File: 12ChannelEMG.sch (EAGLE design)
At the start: 24 parts

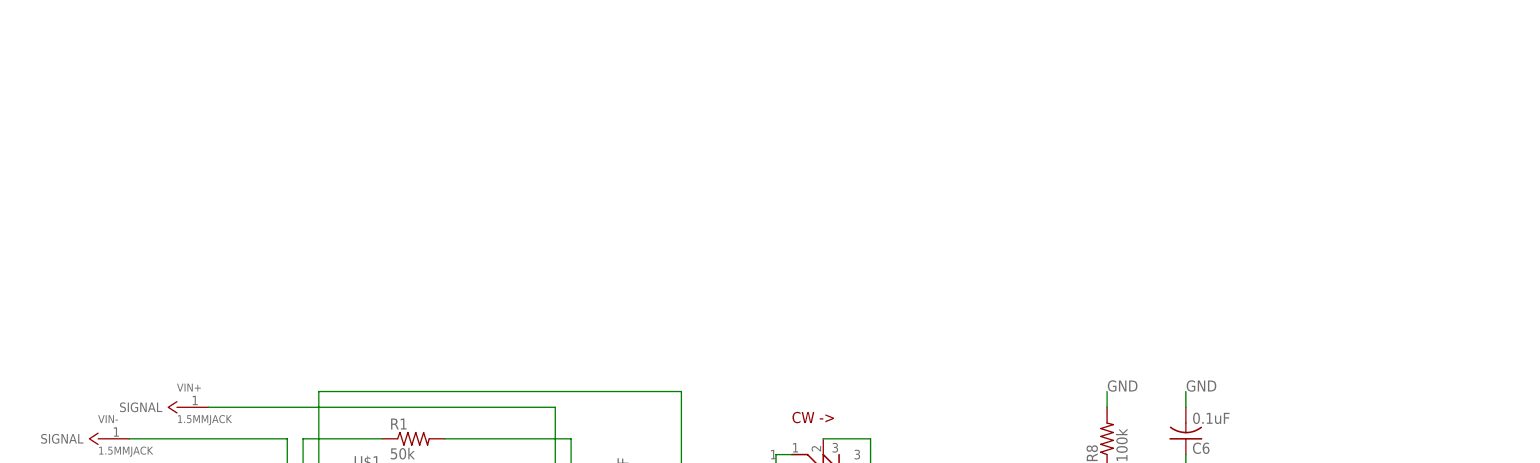
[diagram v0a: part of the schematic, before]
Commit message: Duplicated first channel to make second channel
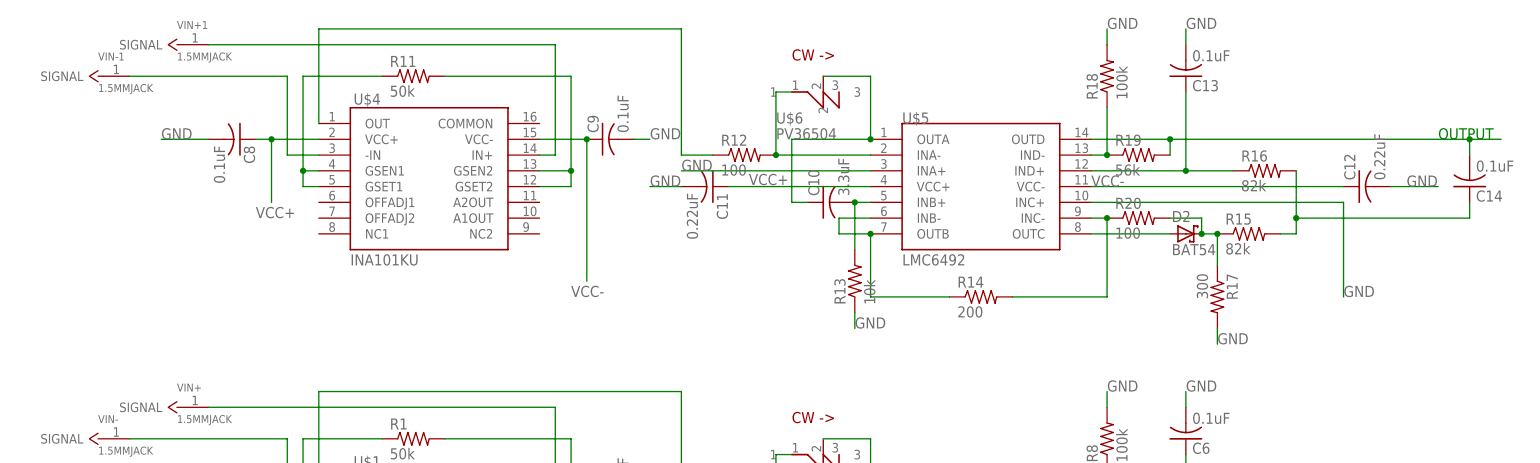
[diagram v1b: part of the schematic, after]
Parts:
- added C10: 3.3uF, resistor:C-USC1206K
- added C11, C12: 0.22uF, rcl:C-USC0603K
- added C13, C14, C8, C9: 0.1uF, resistor:C-USC1206K
- added D2: BAT54, diode:BAT54
- added R11: 50k, rcl:R-US_R0805
- added R12, R20: 100, resistor:R-US_R0603
- added R13: 10k, rcl:R-US_R0603
- added R14: 200, rcl:R-US_R0603
- added R15, R16: 82k, resistor:R-US_R0603
- added R17: 300, resistor:R-US_R0603
- added R18: 100k, resistor:R-US_R0603
- added R19: 56k, resistor:R-US_R0603
- added U$4: INA101KU, 12-ChannelEMG:INA101KUINA101KU
- added U$5: LMC6492, 12-ChannelEMG:LMC6492
- added U$6: PV36504, 12-ChannelEMG:PV36
- added VIN+1, VIN-1: 1.5MMJACK, 12-ChannelEMG:1.5MMJACK
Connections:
- new net N$13: R11.2, U$4.GSEN2, U$4.GSET2
- new net N$20: U$4.-IN, VIN-1.SIGNAL
- new net N$21: R12.2, U$5.INA-, U$6.1
- new net N$22: R12.1, U$4.OUT
- new net N$23: C10.1, U$5.OUTA, U$6.2
- new net N$24: C10.2, R13.2, U$5.INB+
- new net N$25: R14.1, U$5.INB-, U$5.OUTB
- new net N$26: R14.2, R20.1, U$5.INC-
- new net N$27: D2.A, U$5.OUTC
- new net N$28: C13.1, R16.1, U$5.IND+
- new net N$29: D2.C, R15.1, R17.1, R20.2
- new net N$30: C14.2, R19.2, U$5.OUTD
- new net N$31: R18.1, R19.1, U$5.IND-
- new net N$32: C14.1, R15.2, R16.2
- new net N$33: R11.1, U$4.GSEN1, U$4.GSET1
- new net N$34: U$4.IN+, VIN+1.SIGNAL
- net GND: now also C11.2, C12.2, C13.2, C8.2, C9.2, R13.1, R17.2, R18.2, U$5.INA+, U$5.INC+
- net VCC+: now also C11.1, C8.1, U$4.VCC+, U$5.VCC+
- net VCC-: now also C12.1, C9.1, U$4.VCC-, U$5.VCC-

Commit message: Three Channels
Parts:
- added C15, C16, C20, C21: 0.1uF, resistor:C-USC1206K
- added C17: 3.3uF, resistor:C-USC1206K
- added C18, C19: 0.22uF, rcl:C-USC0603K
- added D3: BAT54, diode:BAT54
- added R21: 50k, rcl:R-US_R0805
- added R22, R30: 100, resistor:R-US_R0603
- added R23: 10k, rcl:R-US_R0603
- added R24: 200, rcl:R-US_R0603
- added R25, R26: 82k, resistor:R-US_R0603
- added R27: 300, resistor:R-US_R0603
- added R28: 100k, resistor:R-US_R0603
- added R29: 56k, resistor:R-US_R0603
- added U$7: INA101KU, 12-ChannelEMG:INA101KUINA101KU
- added U$8: LMC6492, 12-ChannelEMG:LMC6492
- added U$9: PV36504, 12-ChannelEMG:PV36
- added VIN+2, VIN-2: 1.5MMJACK, 12-ChannelEMG:1.5MMJACK
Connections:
- new net N$35: R21.2, U$7.GSEN2, U$7.GSET2
- new net N$36: U$7.-IN, VIN-2.SIGNAL
- new net N$37: R22.2, U$8.INA-, U$9.1
- new net N$38: R22.1, U$7.OUT
- new net N$39: C17.1, U$8.OUTA, U$9.2
- new net N$40: C17.2, R23.2, U$8.INB+
- new net N$41: R24.1, U$8.INB-, U$8.OUTB
- new net N$42: R24.2, R30.1, U$8.INC-
- new net N$43: D3.A, U$8.OUTC
- new net N$44: C20.1, R26.1, U$8.IND+
- new net N$45: D3.C, R25.1, R27.1, R30.2
- new net N$46: C21.2, R29.2, U$8.OUTD
- new net N$47: R28.1, R29.1, U$8.IND-
- new net N$48: C21.1, R25.2, R26.2
- new net N$49: R21.1, U$7.GSEN1, U$7.GSET1
- new net N$50: U$7.IN+, VIN+2.SIGNAL
- net GND: now also C15.2, C16.2, C18.2, C19.2, C20.2, R23.1, R27.2, R28.2, U$8.INA+, U$8.INC+
- net VCC+: now also C15.1, C18.1, U$7.VCC+, U$8.VCC+
- net VCC-: now also C16.1, C19.1, U$7.VCC-, U$8.VCC-

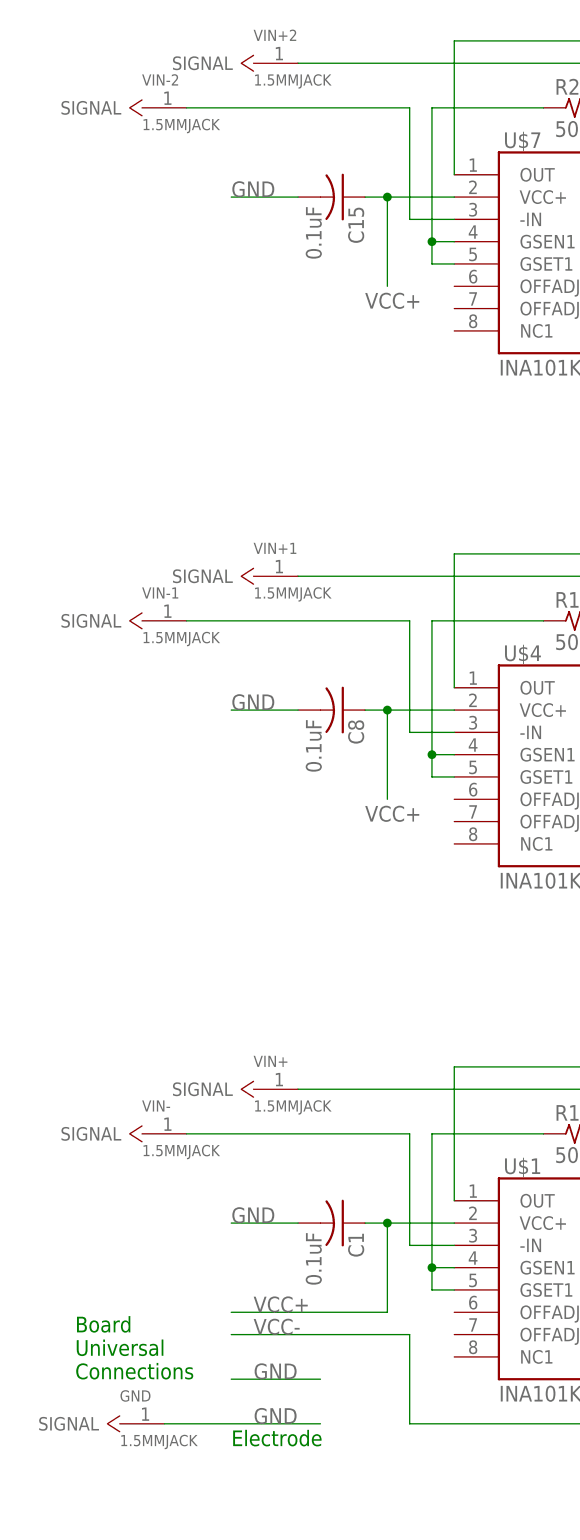
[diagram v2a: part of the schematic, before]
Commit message: Removed old connectors
Added ground jumper for ground electrode
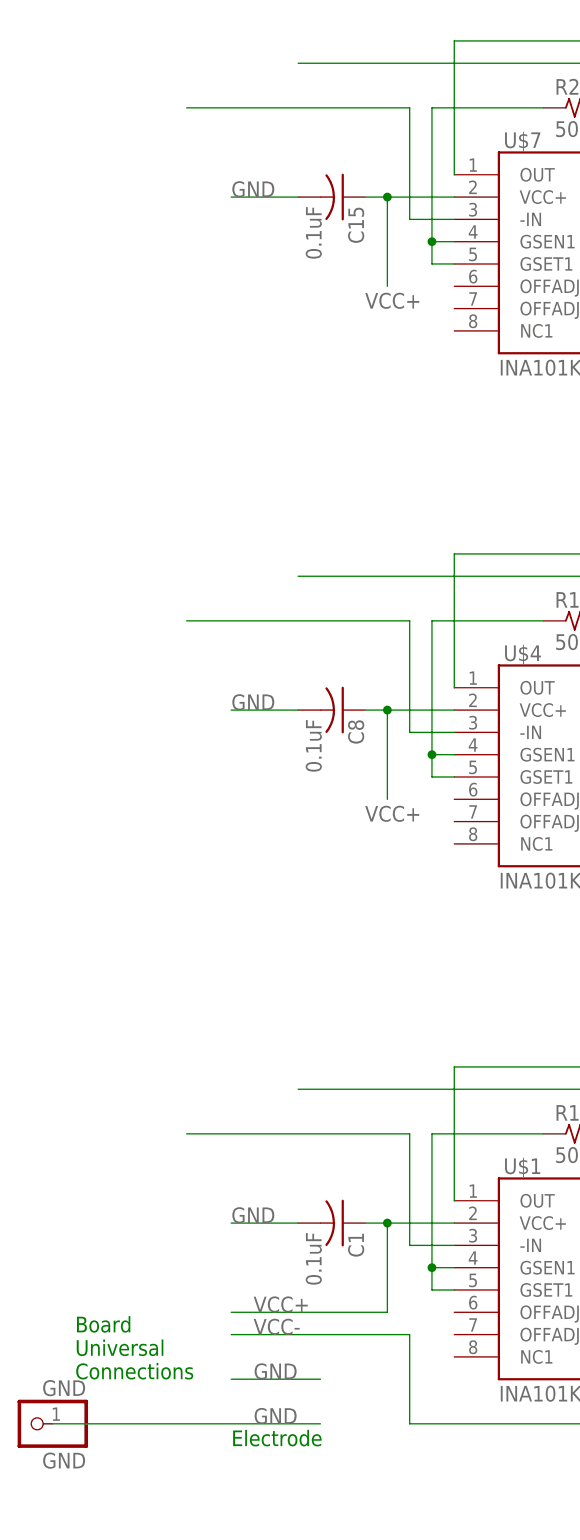
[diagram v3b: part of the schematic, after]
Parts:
- removed VIN+, VIN+1, VIN+2, VIN-, VIN-1, VIN-2: 1.5MMJACK, 12-ChannelEMG:1.5MMJACK
- GND: value 1.5MMJACK -> GND; device 12-ChannelEMG:1.5MMJACK -> pinhead:PINHD-1X1
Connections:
- net GND: now also GND.1; no longer GND.SIGNAL
- net N$20: no longer VIN-1.SIGNAL
- net N$34: no longer VIN+1.SIGNAL
- net N$36: no longer VIN-2.SIGNAL
- net N$50: no longer VIN+2.SIGNAL
- net N$6: no longer VIN-.SIGNAL
- net N$7: no longer VIN+.SIGNAL
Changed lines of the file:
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@@
 <part name="R9" library="resistor" deviceset="R-US_" device="R0603" value="56k"/>
 <part name="R10" library="resistor" deviceset="R-US_" device="R0603" value="100"/>
-<part name="VIN+" library="12-ChannelEMG" deviceset="1.5MMJACK" device=""/>
-<part name="VIN-" library="12-ChannelEMG" deviceset="1.5MMJACK" device=""/>
-<part name="GND" library="12-ChannelEMG" deviceset="1.5MMJACK" device=""/>
 <part name="U$4" library="12-ChannelEMG" deviceset="INA101KU" device="INA101KU" value="INA101KU"/>
 <part name="R11" library="rcl" deviceset="R-US_" device="R0805" value="50k"/>
@@
 <part name="R19" library="resistor" deviceset="R-US_" device="R0603" value="56k"/>
 <part name="R20" library="resistor" deviceset="R-US_" device="R0603" value="100"/>
-<part name="VIN+1" library="12-ChannelEMG" deviceset="1.5MMJACK" device=""/>
-<part name="VIN-1" library="12-ChannelEMG" deviceset="1.5MMJACK" device=""/>
 <part name="U$7" library="12-ChannelEMG" deviceset="INA101KU" device="INA101KU" value="INA101KU"/>
 <part name="R21" library="rcl" deviceset="R-US_" device="R0805" value="50k"/>
@@
 <part name="R29" library="resistor" deviceset="R-US_" device="R0603" value="56k"/>
 <part name="R30" library="resistor" deviceset="R-US_" device="R0603" value="100"/>
-<part name="VIN+2" library="12-ChannelEMG" deviceset="1.5MMJACK" device=""/>
-<part name="VIN-2" library="12-ChannelEMG" deviceset="1.5MMJACK" device=""/>
+<part name="GND" library="pinhead" deviceset="PINHD-1X1" device="" value="GND"/>
 </parts>
 <sheets>
@@
 <instance part="R9" gate="G$1" x="139.7" y="45.72"/>
 <instance part="R10" gate="G$1" x="139.7" y="35.56"/>
-<instance part="VIN+" gate="G$1" x="-17.78" y="63.5"/>
-<instance part="VIN-" gate="G$1" x="-30.48" y="58.42"/>
-<instance part="GND" gate="G$1" x="-33.02" y="25.4"/>
 <instance part="U$4" gate="G$1" x="25.4" y="101.6"/>
 <instance part="R11" gate="G$1" x="22.86" y="116.84"/>
@@
 <instance part="R19" gate="G$1" x="139.7" y="104.14"/>
 <instance part="R20" gate="G$1" x="139.7" y="93.98"/>
-<instance part="VIN+1" gate="G$1" x="-17.78" y="121.92"/>
-<instance part="VIN-1" gate="G$1" x="-30.48" y="116.84"/>
 <instance part="U$7" gate="G$1" x="25.4" y="160.02"/>
 <instance part="R21" gate="G$1" x="22.86" y="175.26"/>
@@
 <instance part="R29" gate="G$1" x="139.7" y="162.56"/>
 <instance part="R30" gate="G$1" x="139.7" y="152.4"/>
-<instance part="VIN+2" gate="G$1" x="-17.78" y="180.34"/>
-<instance part="VIN-2" gate="G$1" x="-30.48" y="175.26"/>
+<instance part="GND" gate="G$1" x="-40.64" y="25.4" rot="MR0"/>
 </instances>
 <busses>
@@
 <wire x1="-17.78" y1="30.48" x2="-7.62" y2="30.48" width="0.1524" layer="91"/>
 <label x="-15.24" y="30.48" size="1.778" layer="95"/>
-<wire x1="-25.4" y1="25.4" x2="-7.62" y2="25.4" width="0.1524" layer="91"/>
+<wire x1="-38.1" y1="25.4" x2="-7.62" y2="25.4" width="0.1524" layer="91"/>
 <label x="-15.24" y="25.4" size="1.778" layer="95"/>
-<pinref part="GND" gate="G$1" pin="SIGNAL"/>
+<pinref part="GND" gate="G$1" pin="1"/>
 </segment>
 <segment>
@@
 <wire x1="2.54" y1="45.72" x2="2.54" y2="58.42" width="0.1524" layer="91"/>
 <wire x1="2.54" y1="58.42" x2="-22.86" y2="58.42" width="0.1524" layer="91"/>
-<pinref part="VIN-" gate="G$1" pin="SIGNAL"/>
 </segment>
 </net>
@@
 <wire x1="43.18" y1="45.72" x2="45.72" y2="45.72" width="0.1524" layer="91"/>
 <wire x1="45.72" y1="45.72" x2="45.72" y2="63.5" width="0.1524" layer="91"/>
-<pinref part="VIN+" gate="G$1" pin="SIGNAL"/>
 <wire x1="45.72" y1="63.5" x2="-10.16" y2="63.5" width="0.1524" layer="91"/>
 </segment>
@@
 <wire x1="2.54" y1="104.14" x2="2.54" y2="116.84" width="0.1524" layer="91"/>
 <wire x1="2.54" y1="116.84" x2="-22.86" y2="116.84" width="0.1524" layer="91"/>
-<pinref part="VIN-1" gate="G$1" pin="SIGNAL"/>
 </segment>
 </net>
@@
 <wire x1="43.18" y1="104.14" x2="45.72" y2="104.14" width="0.1524" layer="91"/>
 <wire x1="45.72" y1="104.14" x2="45.72" y2="121.92" width="0.1524" layer="91"/>
-<pinref part="VIN+1" gate="G$1" pin="SIGNAL"/>
 <wire x1="45.72" y1="121.92" x2="-10.16" y2="121.92" width="0.1524" layer="91"/>
 </segment>
@@
 <wire x1="2.54" y1="162.56" x2="2.54" y2="175.26" width="0.1524" layer="91"/>
 <wire x1="2.54" y1="175.26" x2="-22.86" y2="175.26" width="0.1524" layer="91"/>
-<pinref part="VIN-2" gate="G$1" pin="SIGNAL"/>
 </segment>
 </net>
@@
 <wire x1="43.18" y1="162.56" x2="45.72" y2="162.56" width="0.1524" layer="91"/>
 <wire x1="45.72" y1="162.56" x2="45.72" y2="180.34" width="0.1524" layer="91"/>
-<pinref part="VIN+2" gate="G$1" pin="SIGNAL"/>
 <wire x1="45.72" y1="180.34" x2="-10.16" y2="180.34" width="0.1524" layer="91"/>
 </segment>

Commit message: Two channels, problems fixed
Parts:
- removed C15, C16, C20, C21: 0.1uF, resistor:C-USC1206K
- removed C17: 3.3uF, resistor:C-USC1206K
- removed C18, C19: 0.22uF, rcl:C-USC0603K
- removed D3: BAT54, diode:BAT54
- removed R21: 50k, rcl:R-US_R0805
- removed R22, R30: 100, resistor:R-US_R0603
- removed R23: 10k, rcl:R-US_R0603
- removed R24: 200, rcl:R-US_R0603
- removed R25, R26: 82k, resistor:R-US_R0603
- removed R27: 300, resistor:R-US_R0603
- removed R28: 100k, resistor:R-US_R0603
- removed R29: 56k, resistor:R-US_R0603
- removed U$8: LMC6492, 12-ChannelEMG:LMC6492
- removed U$9: PV36504, 12-ChannelEMG:PV36
- added U$10: 2PIN, 12-ChannelEMG:2PIN
- U$7: value INA101KU -> 2PIN; device 12-ChannelEMG:INA101KUINA101KU -> 12-ChannelEMG:2PIN
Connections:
- removed net N$35: R21.2, U$7.GSEN2, U$7.GSET2
- removed net N$36: U$7.-IN
- removed net N$37: R22.2, U$8.INA-, U$9.1
- removed net N$38: R22.1, U$7.OUT
- removed net N$39: C17.1, U$8.OUTA, U$9.2
- removed net N$40: C17.2, R23.2, U$8.INB+
- removed net N$41: R24.1, U$8.INB-, U$8.OUTB
- removed net N$42: R24.2, R30.1, U$8.INC-
- removed net N$43: D3.A, U$8.OUTC
- removed net N$44: C20.1, R26.1, U$8.IND+
- removed net N$45: D3.C, R25.1, R27.1, R30.2
- removed net N$46: C21.2, R29.2, U$8.OUTD
- removed net N$47: R28.1, R29.1, U$8.IND-
- removed net N$48: C21.1, R25.2, R26.2
- removed net N$49: R21.1, U$7.GSEN1, U$7.GSET1
- removed net N$50: U$7.IN+
- net GND: no longer C15.2, C16.2, C18.2, C19.2, C20.2, R23.1, R27.2, R28.2, U$8.INA+, U$8.INC+
- net N$20: now also U$7.2
- net N$34: now also U$7.1
- net N$6: now also U$10.2
- net N$7: now also U$10.1
- net VCC+: no longer C15.1, C18.1, U$7.VCC+, U$8.VCC+
- net VCC-: no longer C16.1, C19.1, U$7.VCC-, U$8.VCC-
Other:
- moved on the sheet: C10, C11, C12, C13, C14, C8, C9, D2, R11, R12, R13, R14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

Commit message: Channel 4
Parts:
- added C15, C16, C20, C21, C22, C23, C27, C28: 0.1uF, resistor:C-USC1206K
- added C17, C24: 3.3uF, resistor:C-USC1206K
- added C18, C19, C25, C26: 0.22uF, rcl:C-USC0603K
- added D3, D4: BAT54, diode:BAT54
- added R21, R31: 50k, rcl:R-US_R0805
- added R22, R30, R32, R40: 100, resistor:R-US_R0603
- added R23, R33: 10k, rcl:R-US_R0603
- added R24, R34: 200, rcl:R-US_R0603
- added R25, R26, R35, R36: 82k, resistor:R-US_R0603
- added R27, R37: 300, resistor:R-US_R0603
- added R28, R38: 100k, resistor:R-US_R0603
- added R29, R39: 56k, resistor:R-US_R0603
- added U$11, U$15: PV36504, 12-ChannelEMG:PV36
- added U$12, U$16: 2PIN, 12-ChannelEMG:2PIN
- added U$13, U$8: INA101KU, 12-ChannelEMG:INA101KUINA101KU
- added U$14, U$9: LMC6492, 12-ChannelEMG:LMC6492
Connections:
- new net N$35: R21.2, U$8.GSEN2, U$8.GSET2
- new net N$36: U$12.2, U$8.-IN
- new net N$37: R22.2, U$11.1, U$9.INA-
- new net N$38: R22.1, U$8.OUT
- new net N$39: C17.1, U$11.2, U$9.OUTA
- new net N$40: C17.2, R23.2, U$9.INB+
- new net N$41: R24.1, U$9.INB-, U$9.OUTB
- new net N$42: R24.2, R30.1, U$9.INC-
- new net N$43: D3.A, U$9.OUTC
- new net N$44: C20.1, R26.1, U$9.IND+
- new net N$45: D3.C, R25.1, R27.1, R30.2
- new net N$46: C21.2, R29.2, U$9.OUTD
- new net N$47: R28.1, R29.1, U$9.IND-
- new net N$48: C21.1, R25.2, R26.2
- new net N$49: R21.1, U$8.GSEN1, U$8.GSET1
- new net N$50: U$12.1, U$8.IN+
- new net N$51: R31.2, U$13.GSEN2, U$13.GSET2
- new net N$52: U$13.-IN, U$16.2
- new net N$53: R32.2, U$14.INA-, U$15.1
- new net N$54: R32.1, U$13.OUT
- new net N$55: C24.1, U$14.OUTA, U$15.2
- new net N$56: C24.2, R33.2, U$14.INB+
- new net N$57: R34.1, U$14.INB-, U$14.OUTB
- new net N$58: R34.2, R40.1, U$14.INC-
- new net N$59: D4.A, U$14.OUTC
- new net N$60: C27.1, R36.1, U$14.IND+
- new net N$61: D4.C, R35.1, R37.1, R40.2
- new net N$62: C28.2, R39.2, U$14.OUTD
- new net N$63: R38.1, R39.1, U$14.IND-
- new net N$64: C28.1, R35.2, R36.2
- new net N$65: R31.1, U$13.GSEN1, U$13.GSET1
- new net N$66: U$13.IN+, U$16.1
- net GND: now also C15.2, C16.2, C18.2, C19.2, C20.2, C22.2, C23.2, C25.2, C26.2, C27.2, R23.1, R27.2, R28.2, R33.1, R37.2, R38.2, U$14.INA+, U$14.INC+, U$9.INA+, U$9.INC+
- net VCC+: now also C15.1, C18.1, C22.1, C25.1, U$13.VCC+, U$14.VCC+, U$8.VCC+, U$9.VCC+
- net VCC-: now also C16.1, C19.1, C23.1, C26.1, U$13.VCC-, U$14.VCC-, U$8.VCC-, U$9.VCC-

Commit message: Channel 6
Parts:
- added C29, C30, C34, C35, C36, C37, C41, C42: 0.1uF, resistor:C-USC1206K
- added C31, C38: 3.3uF, resistor:C-USC1206K
- added C32, C33, C39, C40: 0.22uF, rcl:C-USC0603K
- added D5, D6: BAT54, diode:BAT54
- added R41, R51: 50k, rcl:R-US_R0805
- added R42, R50, R52, R60: 100, resistor:R-US_R0603
- added R43, R53: 10k, rcl:R-US_R0603
- added R44, R54: 200, rcl:R-US_R0603
- added R45, R46, R55, R56: 82k, resistor:R-US_R0603
- added R47, R57: 300, resistor:R-US_R0603
- added R48, R58: 100k, resistor:R-US_R0603
- added R49, R59: 56k, resistor:R-US_R0603
- added U$17, U$21: INA101KU, 12-ChannelEMG:INA101KUINA101KU
- added U$18, U$22: LMC6492, 12-ChannelEMG:LMC6492
- added U$19, U$23: PV36504, 12-ChannelEMG:PV36
- added U$20, U$24: 2PIN, 12-ChannelEMG:2PIN
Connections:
- new net N$67: R41.2, U$17.GSEN2, U$17.GSET2
- new net N$68: U$17.-IN, U$20.2
- new net N$69: R42.2, U$18.INA-, U$19.1
- new net N$70: R42.1, U$17.OUT
- new net N$71: C31.1, U$18.OUTA, U$19.2
- new net N$72: C31.2, R43.2, U$18.INB+
- new net N$73: R44.1, U$18.INB-, U$18.OUTB
- new net N$74: R44.2, R50.1, U$18.INC-
- new net N$75: D5.A, U$18.OUTC
- new net N$76: C34.1, R46.1, U$18.IND+
- new net N$77: D5.C, R45.1, R47.1, R50.2
- new net N$78: C35.2, R49.2, U$18.OUTD
- new net N$79: R48.1, R49.1, U$18.IND-
- new net N$80: C35.1, R45.2, R46.2
- new net N$81: R41.1, U$17.GSEN1, U$17.GSET1
- new net N$82: U$17.IN+, U$20.1
- new net N$83: R51.2, U$21.GSEN2, U$21.GSET2
- new net N$84: U$21.-IN, U$24.2
- new net N$85: R52.2, U$22.INA-, U$23.1
- new net N$86: R52.1, U$21.OUT
- new net N$87: C38.1, U$22.OUTA, U$23.2
- new net N$88: C38.2, R53.2, U$22.INB+
- new net N$89: R54.1, U$22.INB-, U$22.OUTB
- new net N$90: R54.2, R60.1, U$22.INC-
- new net N$91: D6.A, U$22.OUTC
- new net N$92: C41.1, R56.1, U$22.IND+
- new net N$93: D6.C, R55.1, R57.1, R60.2
- new net N$94: C42.2, R59.2, U$22.OUTD
- new net N$95: R58.1, R59.1, U$22.IND-
- new net N$96: C42.1, R55.2, R56.2
- new net N$97: R51.1, U$21.GSEN1, U$21.GSET1
- new net N$98: U$21.IN+, U$24.1
- net GND: now also C29.2, C30.2, C32.2, C33.2, C34.2, C36.2, C37.2, C39.2, C40.2, C41.2, R43.1, R47.2, R48.2, R53.1, R57.2, R58.2, U$18.INA+, U$18.INC+, U$22.INA+, U$22.INC+
- net VCC+: now also C29.1, C32.1, C36.1, C39.1, U$17.VCC+, U$18.VCC+, U$21.VCC+, U$22.VCC+
- net VCC-: now also C30.1, C33.1, C37.1, C40.1, U$17.VCC-, U$18.VCC-, U$21.VCC-, U$22.VCC-
